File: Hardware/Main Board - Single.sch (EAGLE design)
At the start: 65 parts, among them J1 MICROMOD-2222-C, J10 MICRO-SD-PUSH-PUSH-EXT-PIN, J2 Vertical Qwiic Connector, J4 QWIIC_RIGHT_ANGLE, J5 CORTEX_JTAG_DEBUG_MINIMUM_PTH, J6 MICROMOD_CARRIER, Q1 3.1A/30V/105mΩ, U2 MCP73831, U5 AP7361C-33

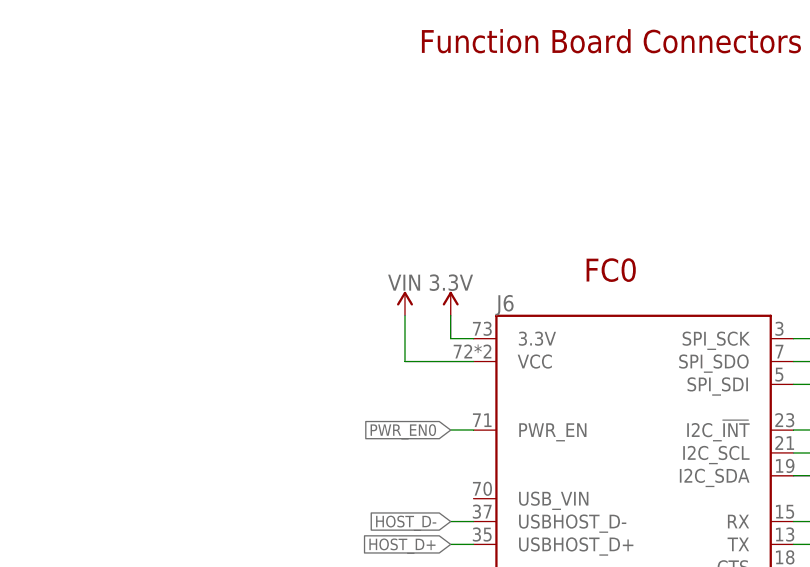
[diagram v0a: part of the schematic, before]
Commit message: Changes power to Function boards @ VCC to VCC and not VIN
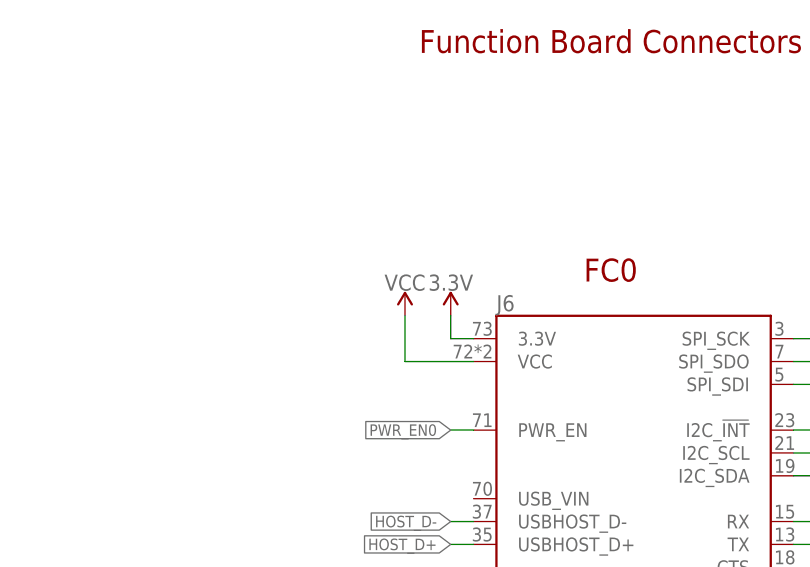
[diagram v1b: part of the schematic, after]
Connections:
- net VCC: now also J6.VCC
- net VIN: no longer J6.VCC
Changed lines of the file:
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@@
 <part name="H4" library="SparkFun-Hardware" deviceset="STAND-OFF-REFLOW" device="-M2.5_2.5MM_TALL"/>
 <part name="GND40" library="SparkFun-PowerSymbols" deviceset="GND" device=""/>
-<part name="SUPPLY9" library="SparkFun-PowerSymbols" deviceset="VIN" device=""/>
 <part name="SUPPLY4" library="SparkFun-PowerSymbols" deviceset="VIN" device=""/>
 <part name="J3" library="SparkFun-Connectors" deviceset="USB_C" device="_2-LAYER_PADS"/>
@@
 <part name="R6" library="SparkFun-Resistors" deviceset="10KOHM" device="-0603-1/10W-1%" value="10k"/>
 <part name="GND6" library="SparkFun-PowerSymbols" deviceset="GND" device=""/>
+<part name="SUPPLY8" library="SparkFun-PowerSymbols" deviceset="VCC" device=""/>
 </parts>
 <sheets>
@@
 <attribute name="VALUE" x="189.484" y="159.004" size="1.778" layer="96" font="vector" align="top-center"/>
 </instance>
-<instance part="SUPPLY9" gate="G$1" x="66.04" y="238.76" smashed="yes">
-<attribute name="VALUE" x="66.04" y="241.554" size="1.778" layer="96" align="bottom-center"/>
-</instance>
 <instance part="SUPPLY4" gate="G$1" x="40.64" y="60.96" smashed="yes">
 <attribute name="VALUE" x="40.64" y="63.754" size="1.778" layer="96" align="bottom-center"/>
@@
 <instance part="GND6" gate="1" x="266.7" y="218.44" smashed="yes">
 <attribute name="VALUE" x="266.7" y="218.186" size="1.778" layer="96" align="top-center"/>
+</instance>
+<instance part="SUPPLY8" gate="G$1" x="66.04" y="238.76" smashed="yes">
+<attribute name="VALUE" x="66.04" y="241.554" size="1.778" layer="96" align="bottom-center"/>
 </instance>
 </instances>
@@
 </net>
 <net name="VIN" class="0">
-<segment>
-<pinref part="SUPPLY9" gate="G$1" pin="VIN"/>
-<wire x1="66.04" y1="233.68" x2="66.04" y2="238.76" width="0.1524" layer="91"/>
-<pinref part="J6" gate="J1" pin="VCC"/>
-<wire x1="73.66" y1="233.68" x2="66.04" y2="233.68" width="0.1524" layer="91"/>
-</segment>
 <segment>
 <pinref part="R10" gate="G$1" pin="2"/>
@@
 <pinref part="SUPPLY6" gate="G$1" pin="VCC"/>
 </segment>
-</net>
+<segment>
+<wire x1="66.04" y1="233.68" x2="66.04" y2="238.76" width="0.1524" layer="91"/>
+<pinref part="J6" gate="J1" pin="VCC"/>
+<wire x1="73.66" y1="233.68" x2="66.04" y2="233.68" width="0.1524" layer="91"/>
+<pinref part="SUPPLY8" gate="G$1" pin="VCC"/>
+</segment>
+</net>

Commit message: Rolls to V11
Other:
- note added: "v11"
- note removed: "v10"
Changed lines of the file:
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@@
 <text x="88.9" y="269.24" size="2.54" layer="94" font="vector" align="center">Function Board Connectors</text>
 <text x="99.06" y="144.78" size="2.54" layer="94" font="vector" align="center">Processor Board Connector</text>
-<text x="424.18" y="7.62" size="2.54" layer="94" font="vector" align="center">v10</text>
+<text x="424.18" y="7.62" size="2.54" layer="94" font="vector" align="center">v11</text>
 <text x="266.7" y="104.14" size="2.54" layer="94" font="vector" align="center">microSD Card</text>
 <text x="401.32" y="185.42" size="2.54" layer="94" font="vector" align="center">Connectors</text>

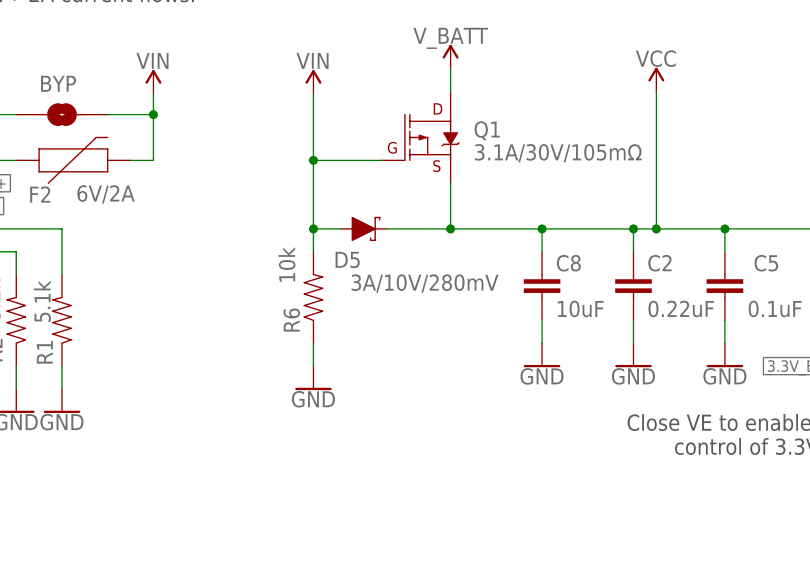
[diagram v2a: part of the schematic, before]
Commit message: Replaces shottky diode
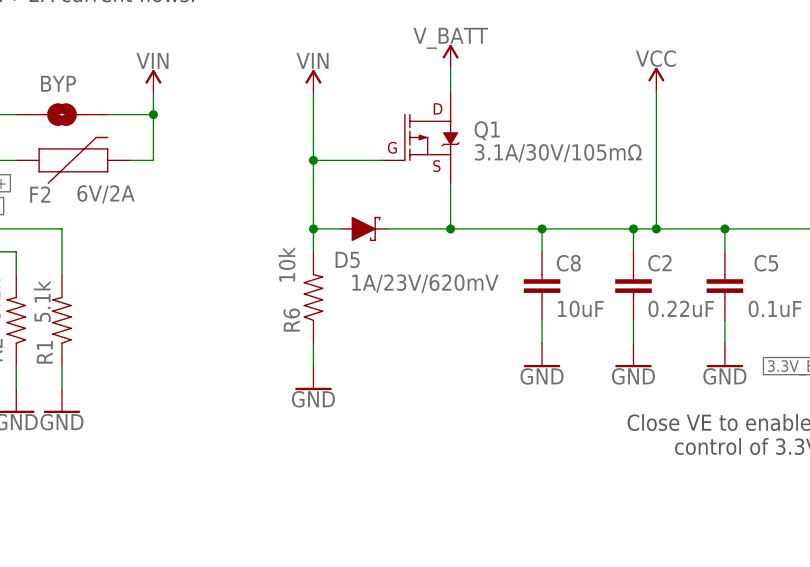
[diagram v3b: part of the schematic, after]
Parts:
- D5: value 3A/10V/280mV -> 1A/23V/620mV; device SparkFun-DiscreteSemi:DIODE-SCHOTTKY-BAT60A -> SparkFun-DiscreteSemi:DIODE-SCHOTTKY-BAT20J
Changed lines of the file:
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@@
 <part name="C8" library="SparkFun-Capacitors" deviceset="10UF" device="-0805-10V-10%" value="10uF"/>
 <part name="SUPPLY28" library="SparkFun-PowerSymbols" deviceset="VCC" device=""/>
-<part name="D5" library="SparkFun-DiscreteSemi" deviceset="DIODE-SCHOTTKY" device="-BAT60A" value="3A/10V/280mV"/>
+<part name="D5" library="SparkFun-DiscreteSemi" deviceset="DIODE-SCHOTTKY" device="-BAT20J" value="1A/23V/620mV"/>
 <part name="5V_LED" library="SparkFun-Jumpers" deviceset="JUMPER-SMT_2_NC_TRACE" device="_SILK" package3d_urn="urn:adsk.eagle:package:39281/1" value=""/>
 <part name="R8" library="SparkFun-Resistors" deviceset="4.7KOHM" device="-0603-1/10W-1%" value="4.7k"/>

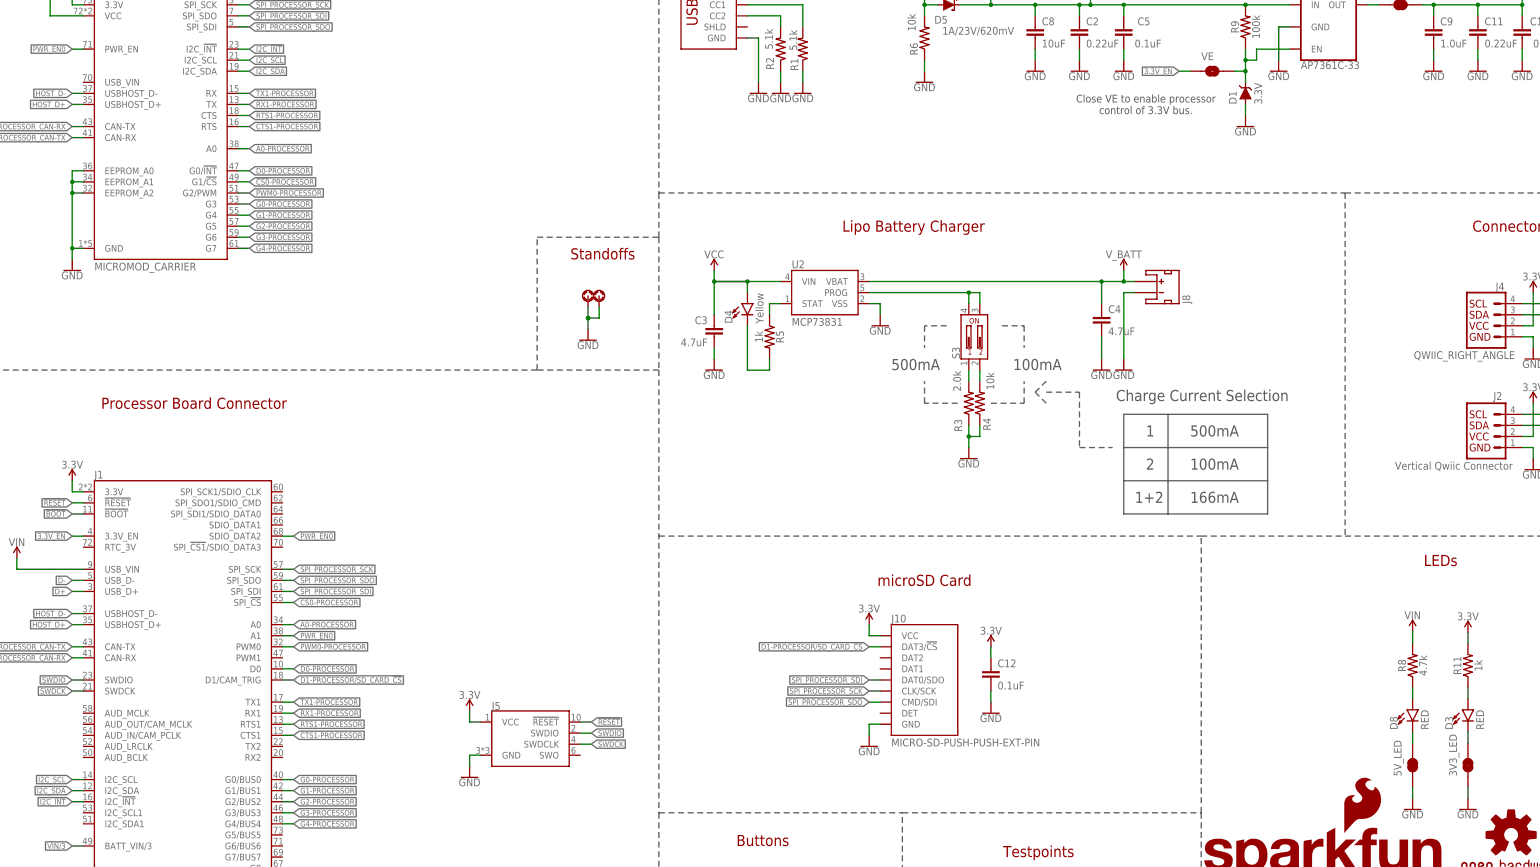
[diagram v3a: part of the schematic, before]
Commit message: Updates function board symbol, fixes charging current value when 1 and 2 are flipped.
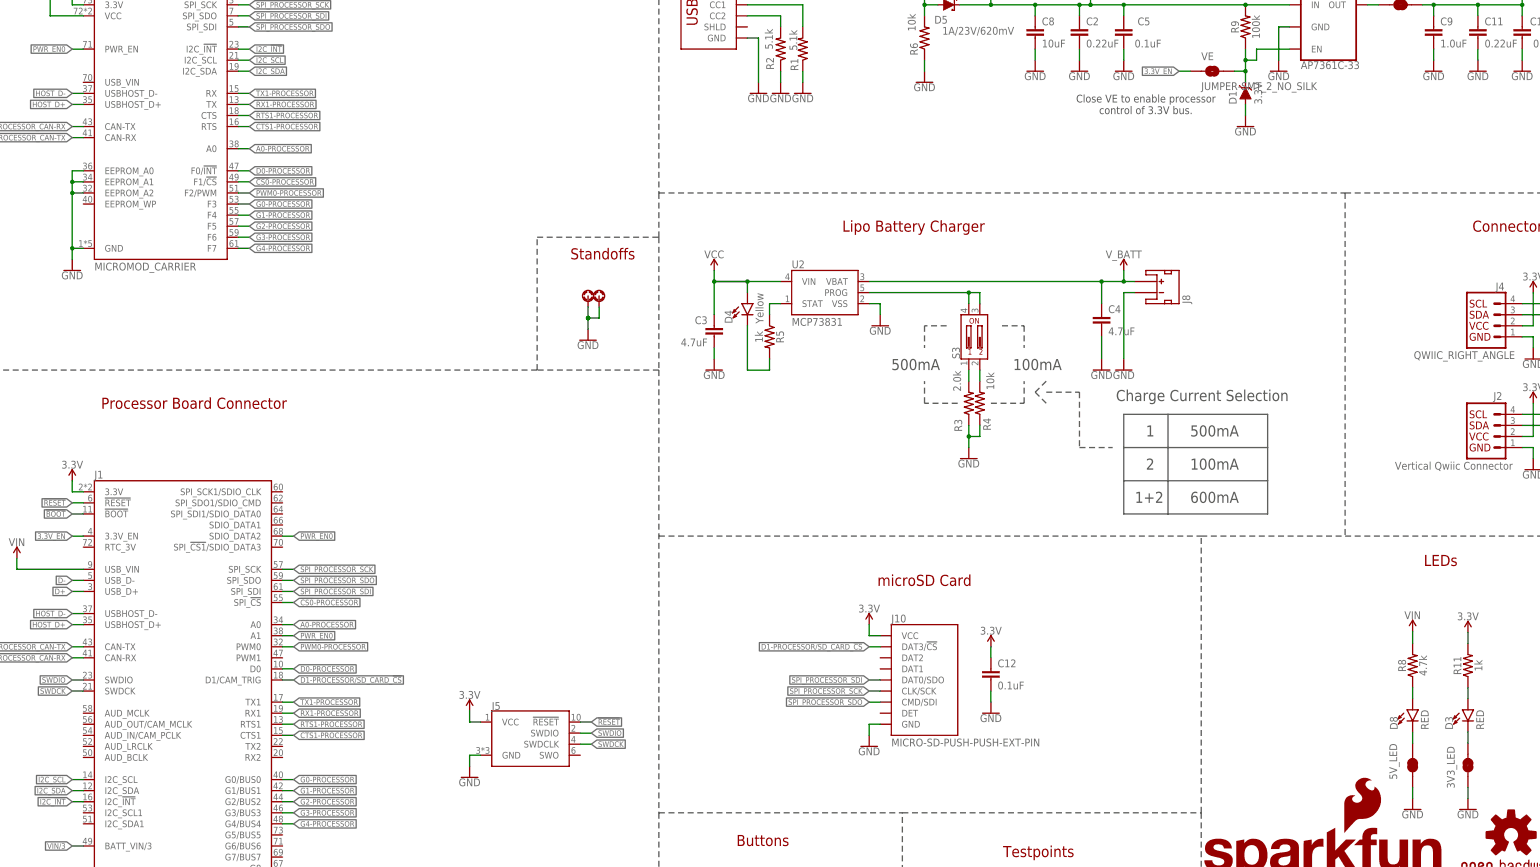
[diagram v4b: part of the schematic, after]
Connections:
- net !CS0!-PROCESSOR: now also J6.F1/!CS!; no longer J6.G1/!CS!
- net D0-PROCESSOR: now also J6.F0/!INT!; no longer J6.G0/!INT!
- net G0-PROCESSOR: now also J6.F3; no longer J6.G3
- net G1-PROCESSOR: now also J6.F4; no longer J6.G4
- net G2-PROCESSOR: now also J6.F5; no longer J6.G5
- net G3-PROCESSOR: now also J6.F6; no longer J6.G6
- net G4-PROCESSOR: now also J6.F7; no longer J6.G7
- net PWM0-PROCESSOR: now also J6.F2/PWM; no longer J6.G2/PWM
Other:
- note added: "600mA"
- note removed: "166mA"
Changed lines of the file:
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@@
 <part name="GND34" library="SparkFun-PowerSymbols" deviceset="GND" device=""/>
 <part name="GND35" library="SparkFun-PowerSymbols" deviceset="GND" device=""/>
-<part name="VE" library="SparkFun-Jumpers" deviceset="JUMPER-SMT_2_NO" device="_SILK" package3d_urn="urn:adsk.eagle:package:39279/1" value=""/>
-<part name="3V3_LED" library="SparkFun-Jumpers" deviceset="JUMPER-SMT_2_NC_TRACE" device="_SILK" package3d_urn="urn:adsk.eagle:package:39281/1" value=""/>
+<part name="VE" library="SparkFun-Jumpers" deviceset="JUMPER-SMT_2_NO" device="_SILK" package3d_urn="urn:adsk.eagle:package:39279/1" value="JUMPER-SMT_2_NO_SILK"/>
+<part name="3V3_LED" library="SparkFun-Jumpers" deviceset="JUMPER-SMT_2_NC_TRACE" device="_SILK" package3d_urn="urn:adsk.eagle:package:39281/1" value="JUMPER-SMT_2_NC_TRACE_SILK"/>
 <part name="R11" library="SparkFun-Resistors" deviceset="1KOHM" device="-0603-1/10W-1%" value="1k"/>
 <part name="D3" library="SparkFun-LED" deviceset="LED-RED" device="0603" value="RED"/>
@@
 <part name="SUPPLY28" library="SparkFun-PowerSymbols" deviceset="VCC" device=""/>
 <part name="D5" library="SparkFun-DiscreteSemi" deviceset="DIODE-SCHOTTKY" device="-BAT20J" value="1A/23V/620mV"/>
-<part name="5V_LED" library="SparkFun-Jumpers" deviceset="JUMPER-SMT_2_NC_TRACE" device="_SILK" package3d_urn="urn:adsk.eagle:package:39281/1" value=""/>
+<part name="5V_LED" library="SparkFun-Jumpers" deviceset="JUMPER-SMT_2_NC_TRACE" device="_SILK" package3d_urn="urn:adsk.eagle:package:39281/1" value="JUMPER-SMT_2_NC_TRACE_SILK"/>
 <part name="R8" library="SparkFun-Resistors" deviceset="4.7KOHM" device="-0603-1/10W-1%" value="4.7k"/>
 <part name="D8" library="SparkFun-LED" deviceset="LED-RED" device="0603" value="RED"/>
@@
 <wire x1="312.42" y1="127" x2="345.44" y2="127" width="0.2032" layer="97"/>
 <text x="314.96" y="121.92" size="2.54" layer="97" font="vector">1+2</text>
-<text x="327.66" y="121.92" size="2.54" layer="97" font="vector">166mA</text>
 <wire x1="294.64" y1="147.32" x2="302.26" y2="147.32" width="0.2032" layer="97" style="dashdot"/>
 <wire x1="302.26" y1="147.32" x2="302.26" y2="134.62" width="0.2032" layer="97" style="dashdot"/>
@@
 <wire x1="330.2" y1="50.8" x2="330.2" y2="114.3" width="0.2032" layer="97" style="longdash"/>
 <wire x1="261.62" y1="0" x2="261.62" y2="50.8" width="0.2032" layer="97" style="longdash"/>
+<text x="327.66" y="121.92" size="2.54" layer="97" font="vector">600mA</text>
 </plain>
 <instances>
@@
 </instance>
 <instance part="3V3_LED" gate="G$1" x="391.414" y="61.722" smashed="yes" rot="R90">
-<attribute name="NAME" x="388.874" y="59.182" size="1.778" layer="95" font="vector" rot="R90"/>
-<attribute name="VALUE" x="393.954" y="59.182" size="1.778" layer="96" font="vector" rot="R90" align="top-left"/>
+<attribute name="NAME" x="388.366" y="56.388" size="1.778" layer="95" font="vector" rot="R90"/>
 </instance>
 <instance part="R11" gate="G$1" x="391.414" y="84.582" smashed="yes" rot="R90">
@@
 </instance>
 <instance part="5V_LED" gate="G$1" x="378.714" y="61.722" smashed="yes" rot="R90">
-<attribute name="NAME" x="376.174" y="59.182" size="1.778" layer="95" font="vector" rot="R90"/>
-<attribute name="VALUE" x="381.254" y="59.182" size="1.778" layer="96" font="vector" rot="R90" align="top-left"/>
+<attribute name="NAME" x="375.158" y="58.42" size="1.778" layer="95" font="vector" rot="R90"/>
 </instance>
 <instance part="R8" gate="G$1" x="378.714" y="84.582" smashed="yes" rot="R90">
@@
 <wire x1="109.22" y1="190.5" x2="111.76" y2="190.5" width="0.1524" layer="91"/>
 <label x="111.76" y="190.5" size="1.27" layer="95" font="vector" xref="yes"/>
-<pinref part="J6" gate="J1" pin="G3"/>
+<pinref part="J6" gate="J1" pin="F3"/>
 </segment>
 </net>
@@
 <wire x1="109.22" y1="187.96" x2="111.76" y2="187.96" width="0.1524" layer="91"/>
 <label x="111.76" y="187.96" size="1.27" layer="95" font="vector" xref="yes"/>
-<pinref part="J6" gate="J1" pin="G4"/>
+<pinref part="J6" gate="J1" pin="F4"/>
 </segment>
 </net>
@@
 <wire x1="109.22" y1="185.42" x2="111.76" y2="185.42" width="0.1524" layer="91"/>
 <label x="111.76" y="185.42" size="1.27" layer="95" font="vector" xref="yes"/>
-<pinref part="J6" gate="J1" pin="G5"/>
+<pinref part="J6" gate="J1" pin="F5"/>
 </segment>
 </net>
@@
 <wire x1="109.22" y1="182.88" x2="111.76" y2="182.88" width="0.1524" layer="91"/>
 <label x="111.76" y="182.88" size="1.27" layer="95" font="vector" xref="yes"/>
-<pinref part="J6" gate="J1" pin="G6"/>
+<pinref part="J6" gate="J1" pin="F6"/>
 </segment>
 </net>
@@
 <wire x1="109.22" y1="180.34" x2="111.76" y2="180.34" width="0.1524" layer="91"/>
 <label x="111.76" y="180.34" size="1.27" layer="95" font="vector" xref="yes"/>
-<pinref part="J6" gate="J1" pin="G7"/>
+<pinref part="J6" gate="J1" pin="F7"/>
 </segment>
 </net>
@@
 </segment>
 <segment>
-<pinref part="J6" gate="J1" pin="G1/!CS!"/>
+<pinref part="J6" gate="J1" pin="F1/!CS!"/>
 <wire x1="109.22" y1="195.58" x2="111.76" y2="195.58" width="0.1524" layer="91"/>
 <label x="111.76" y="195.58" size="1.27" layer="95" font="vector" xref="yes"/>
@@
 </segment>
 <segment>
-<pinref part="J6" gate="J1" pin="G0/!INT!"/>
+<pinref part="J6" gate="J1" pin="F0/!INT!"/>
 <wire x1="109.22" y1="198.12" x2="111.76" y2="198.12" width="0.1524" layer="91"/>
 <label x="111.76" y="198.12" size="1.27" layer="95" font="vector" xref="yes"/>
@@
 </segment>
 <segment>
-<pinref part="J6" gate="J1" pin="G2/PWM"/>
+<pinref part="J6" gate="J1" pin="F2/PWM"/>
 <wire x1="109.22" y1="193.04" x2="111.76" y2="193.04" width="0.1524" layer="91"/>
 <label x="111.76" y="193.04" size="1.27" layer="95" font="vector" xref="yes"/>

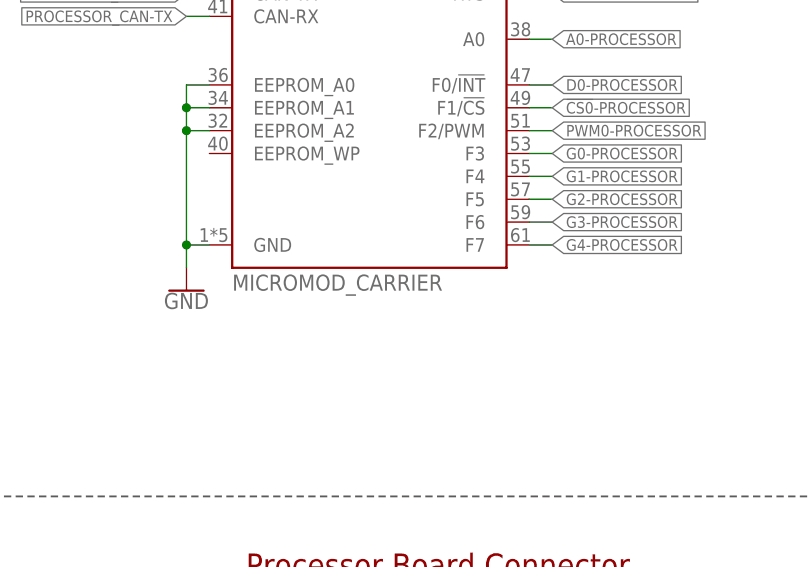
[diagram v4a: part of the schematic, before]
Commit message: Updates the design to use the Micromod-function device in the official SFE Eagle Libs
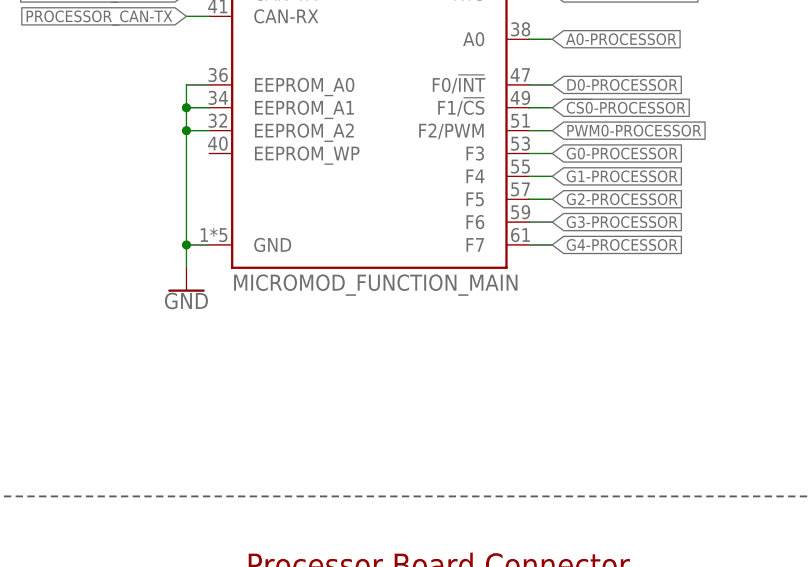
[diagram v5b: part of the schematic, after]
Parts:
- J6: value MICROMOD_CARRIER -> MICROMOD_FUNCTION_MAIN; device SparkFun-MicroMod-Function:MICROMOD_CARRIER -> SparkFun-MicroMod:MICROMOD_FUNCTION_MAIN
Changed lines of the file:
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@@
 <?xml version="1.0" encoding="utf-8"?>
 <!DOCTYPE eagle SYSTEM "eagle.dtd">
-<eagle version="9.6.2">
+<eagle version="9.5.1">
 <drawing>
 <settings>
@@
 <part name="R10" library="SparkFun-Resistors" deviceset="20KOHM" device="-0603-1/10W-1%" value="20k"/>
 <part name="GND23" library="SparkFun-PowerSymbols" deviceset="GND" device=""/>
-<part name="J6" library="SparkFun-MicroMod-Function" deviceset="MICROMOD" device="_CARRIER" value="MICROMOD_CARRIER"/>
+<part name="J6" library="SparkFun-MicroMod" deviceset="MICROMOD_FUNCTION" device="_MAIN" value="MICROMOD_FUNCTION_MAIN"/>
 <part name="J10" library="SparkFun-Connectors" deviceset="MICRO-SD" device="-PUSH-PUSH-EXT-PIN"/>
 <part name="SUPPLY25" library="SparkFun-PowerSymbols" deviceset="3.3V" device=""/>
